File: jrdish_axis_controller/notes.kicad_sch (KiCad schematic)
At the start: 0 parts

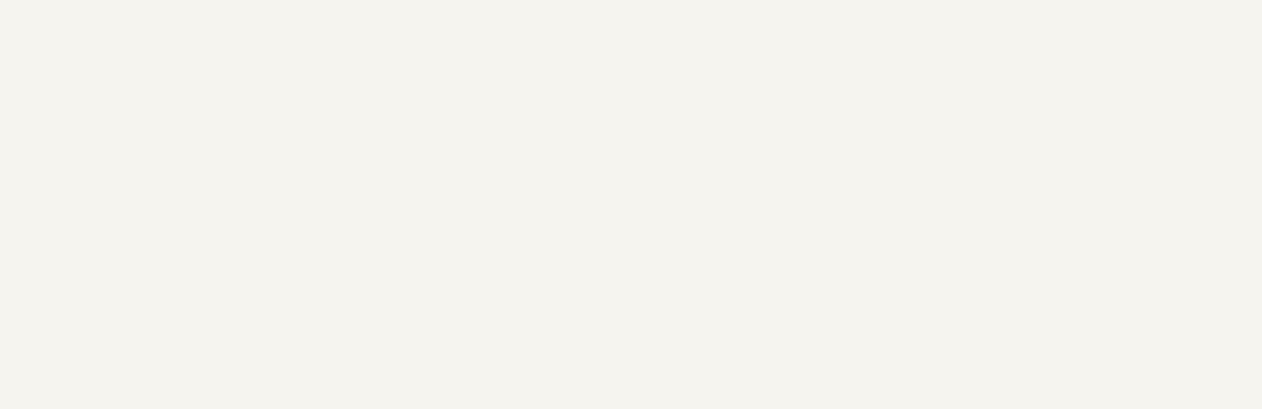
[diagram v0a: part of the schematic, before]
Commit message: Updates for replacing 10k resistors and encoder RC.
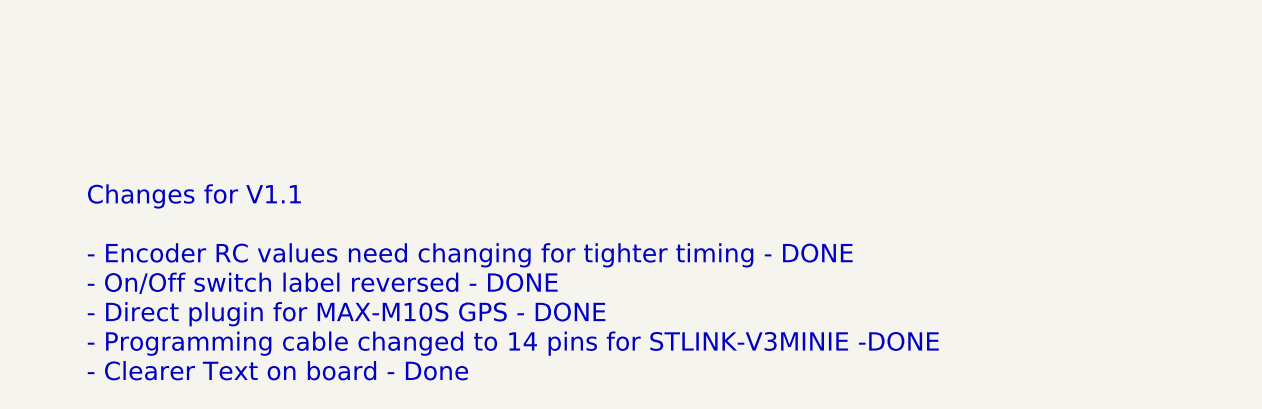
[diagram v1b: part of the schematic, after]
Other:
- note added: "Changes for V1.1 - Encoder RC values need changing for tighter timing - DONE - On/Off switch label reversed - DONE - Direct plugin for MAX-M10S GPS - DONE - Programming cable changed to 14 pins for STLINK-V3MINIE -DONE - Clearer Text on board - Done"
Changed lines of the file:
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@@
 	(title_block
 		(title "Notes")
-		(date "2026-04-30")
-		(rev "1.0")
+		(date "2026-07-11")
+		(rev "1.1")
 		(company "JRSeti")
 	)
@@
 			)
 			(justify left)
+		)
+	)
+	(text "Changes for V1.1\n\n- Encoder RC values need changing for tighter timing - DONE\n- On/Off switch label reversed - DONE\n- Direct plugin for MAX-M10S GPS - DONE\n- Programming cable changed to 14 pins for STLINK-V3MINIE -DONE\n- Clearer Text on board - Done"
+		(exclude_from_sim no)
+		(at 28.194 155.194 0)
+		(effects
+			(font
+				(size 2.032 2.032)
+			)
+			(justify left)
